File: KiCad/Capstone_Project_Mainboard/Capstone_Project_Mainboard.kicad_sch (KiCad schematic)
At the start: 0 parts

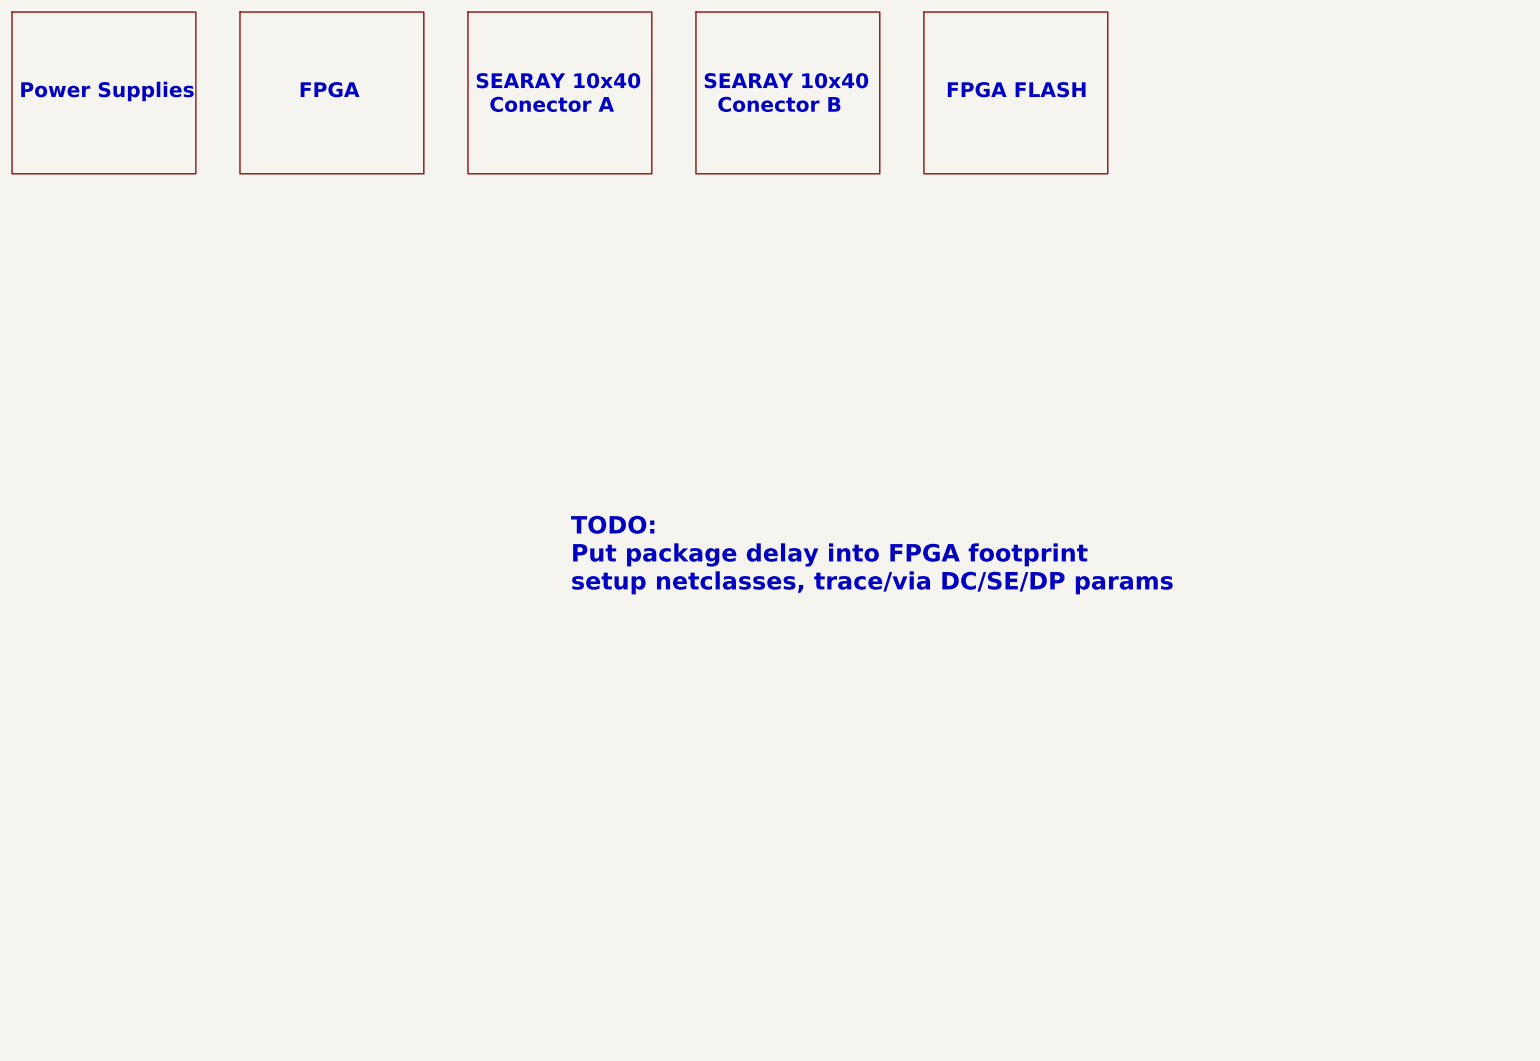
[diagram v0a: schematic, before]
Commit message: Updated FPGA Footprint
Added die-to-pad length offsets to all pins of the FFG676 package. These values were derived from the delay files provided in Vivado.
+ Other minor bugfixes
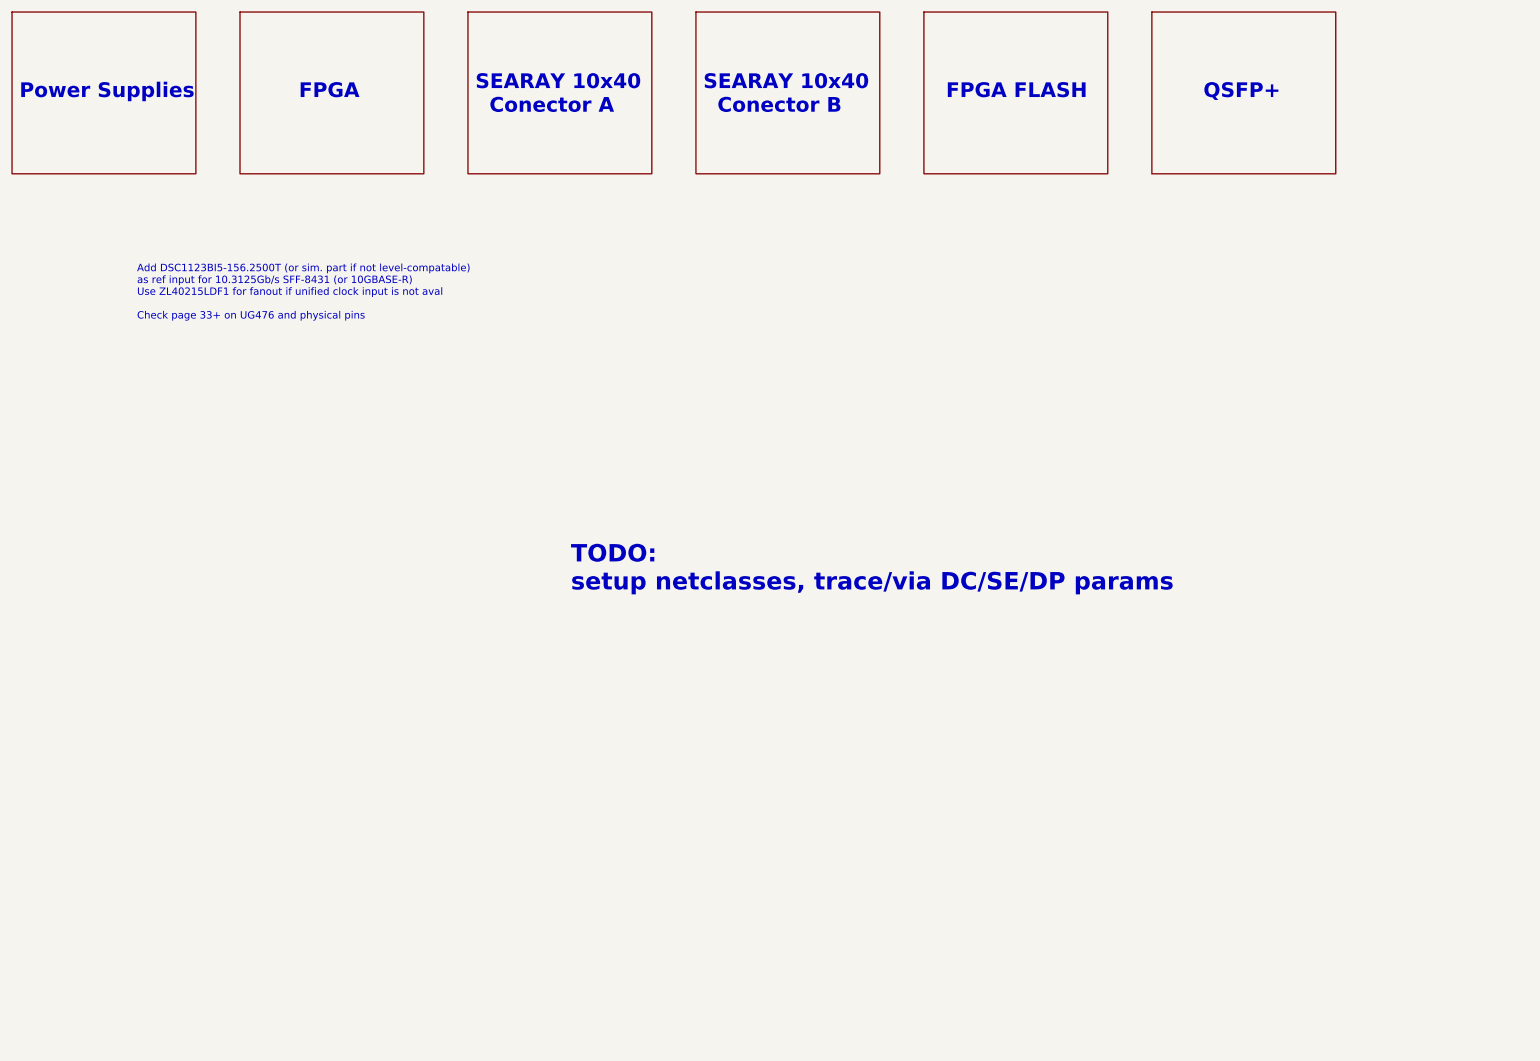
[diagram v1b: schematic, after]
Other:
- added sheet QSFP+ (QSFP2.kicad_sch)
- note added: "Add DSC1123BI5-156.2500T (or sim. part if not level-compatable) as ref input for 10.3125Gb/s SFF-8431 (or 10GBASE-R) Use ZL40215LDF1 for fanout if unified clock input is not aval Check page 33+ on UG476 and physical pins"
- note added: "QSFP+"
- note added: "TODO: setup netclasses, trace/via DC/SE/DP params"
- note removed: "TODO: Put package delay into FPGA footprint setup netclasses, trace/via DC/SE/DP params"
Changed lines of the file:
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@@
   (title_block
     (title "TBD ")
-    (date "2023-12-18")
+    (date "2023-12-22")
     (rev "A")
     (company "Jordan Harris-Toovy")
     (comment 1 "Mainboard for Capstone Project at Oregon Tech")
   )
-  (text "TODO:\nPut package delay into FPGA footprint\nsetup netclasses, trace/via DC/SE/DP params"
-    (at 114.3 116.84 0)
+  (text "TODO:\nsetup netclasses, trace/via DC/SE/DP params" (at 114.3 116.84 0)
     (effects (font (size 3 3) (thickness 0.6) bold) (justify left bottom))
   )
@@
     (effects (font (size 2.54 2.54) (thickness 0.254) bold) (justify left bottom))
   )
+  (text "QSFP+" (at 223.52 31.75 0)
+    (effects (font (size 2.54 2.54) (thickness 0.254) bold) (justify left bottom))
+  )
   (text "Power Supplies" (at 19.05 31.75 0)
     (effects (font (size 2.54 2.54) (thickness 0.254) bold) (justify left bottom))
+  )
+  (text "Add DSC1123BI5-156.2500T (or sim. part if not level-compatable)\nas ref input for 10.3125Gb/s SFF-8431 (or 10GBASE-R)\nUse ZL40215LDF1 for fanout if unified clock input is not aval\n\nCheck page 33+ on UG476 and physical pins"
+    (at 39.37 69.85 0)
+    (effects (font (size 1.27 1.27)) (justify left bottom))
   )
   (text "SEARAY 10x40\n  Conector A" (at 97.79 34.29 0)
@@
       )
     )
+  )
+  (sheet (at 214.63 16.51) (size 31.75 27.94) (fields_autoplaced)
+    (stroke (width 0.1524) (type solid))
+    (fill (color 0 0 0 0.0000))
+    (property "Sheetname" "QSFP+" (at 214.63 15.7984 0)
+      (effects (font (size 1.27 1.27)) (justify left bottom) hide)
+    )
+    (property "Sheetfile" "QSFP2.kicad_sch" (at 214.63 45.0346 0)
+      (effects (font (size 1.27 1.27)) (justify left top) hide)
+    )
+    (instances
+      (project "Capstone_Project_Mainboard"
+        (path "/6eda7ca5-0c45-42b1-905b-ff38fc3c0c32" (page "19"))
+      )
+    )

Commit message: Core non-power parts defined
Most major non-power components added to KiCad project
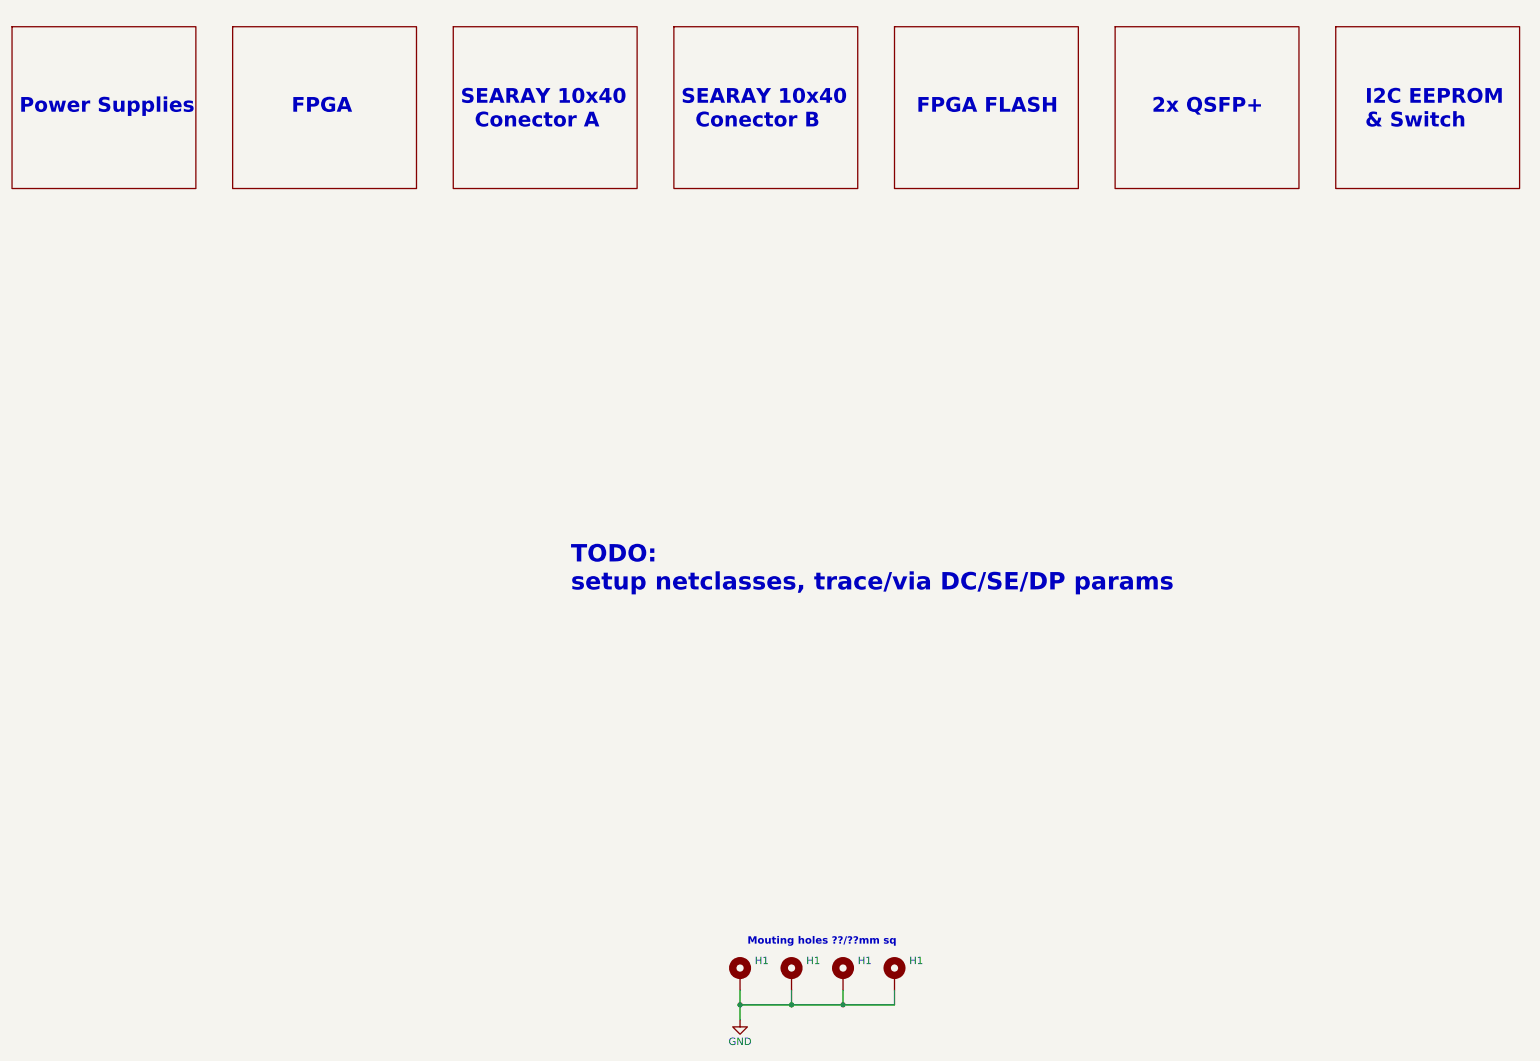
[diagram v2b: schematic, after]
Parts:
- added H1 (x4): Main MH, MountingHole:MountingHole_2.5mm_Pad, symbol Mechanical:MountingHole_Pad
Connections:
- new net GND: H1.1, H1.1, H1.1, H1.1
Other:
- added sheet I2C EEPROM & Switch (I2C_EEPROM_Switch.kicad_sch)
- note added: "2x QSFP+"
- note added: "I2C EEPROM & Switch"
- note added: "Mouting holes ??/??mm sq"
- note removed: "Add DSC1123BI5-156.2500T (or sim. part if not level-compatable) as ref input for 10.3125Gb/s SFF-8431 (or 10GBASE-R) Use ZL40215LDF1 for fanout if unified clock input is not aval Check page 33+ on UG476 and physical pins"
- note removed: "QSFP+"
